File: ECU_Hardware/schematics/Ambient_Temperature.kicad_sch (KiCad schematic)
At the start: 0 parts

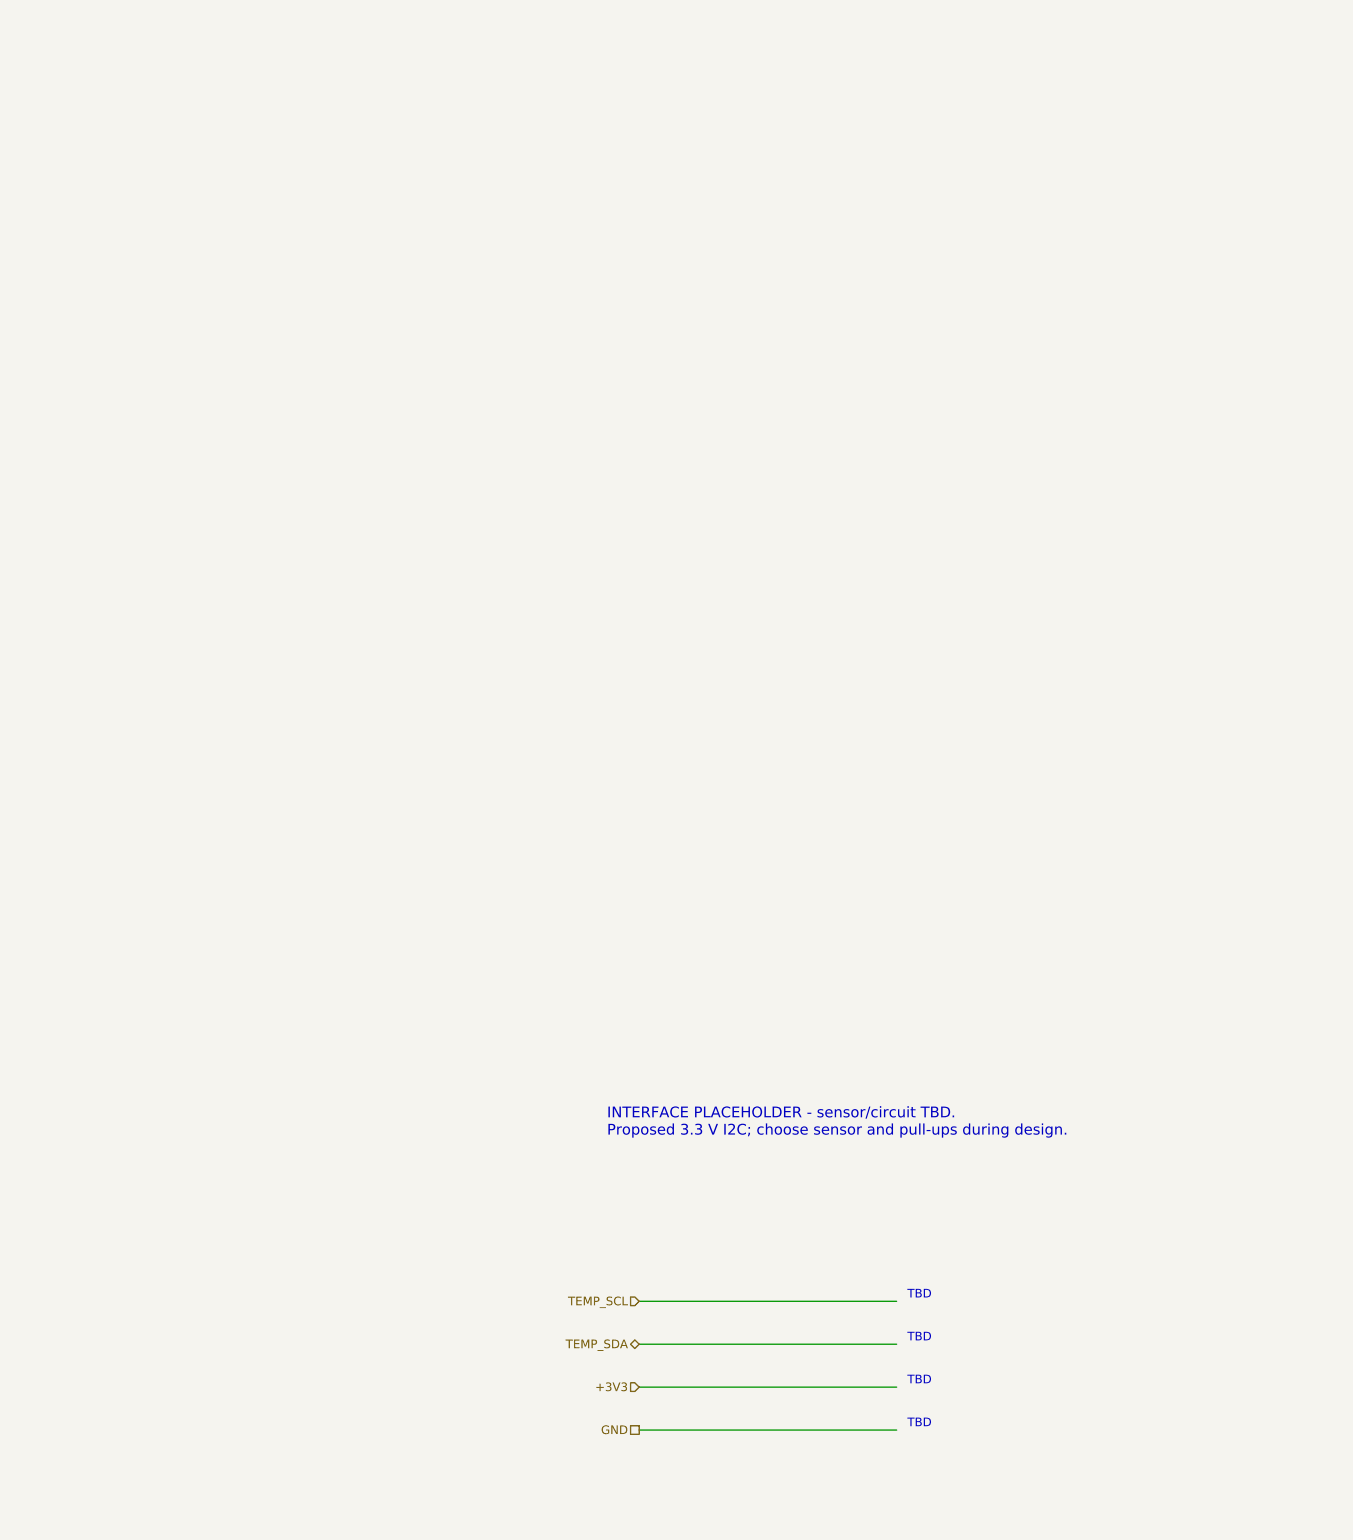
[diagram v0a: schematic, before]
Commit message: Move ECU schematics into schematics/ and add driver inputs and sensor notes
Hierarchical sheets now live in ECU_Hardware/schematics, with the new
Driver_Inputs sheet (APPS, BPPS and steering dividers and clamps), the
reviewed and JLCPCB project symbol libraries, new 3D models, and
SENSOR_INTERFACES.md with the GPS, IMU and temperature pin allocation.
The old top-level sheets and the restore backup are removed.

Claude-Session: https://claude.ai/code/session_0117trEbCv7z6CPYkN3K3GKQ
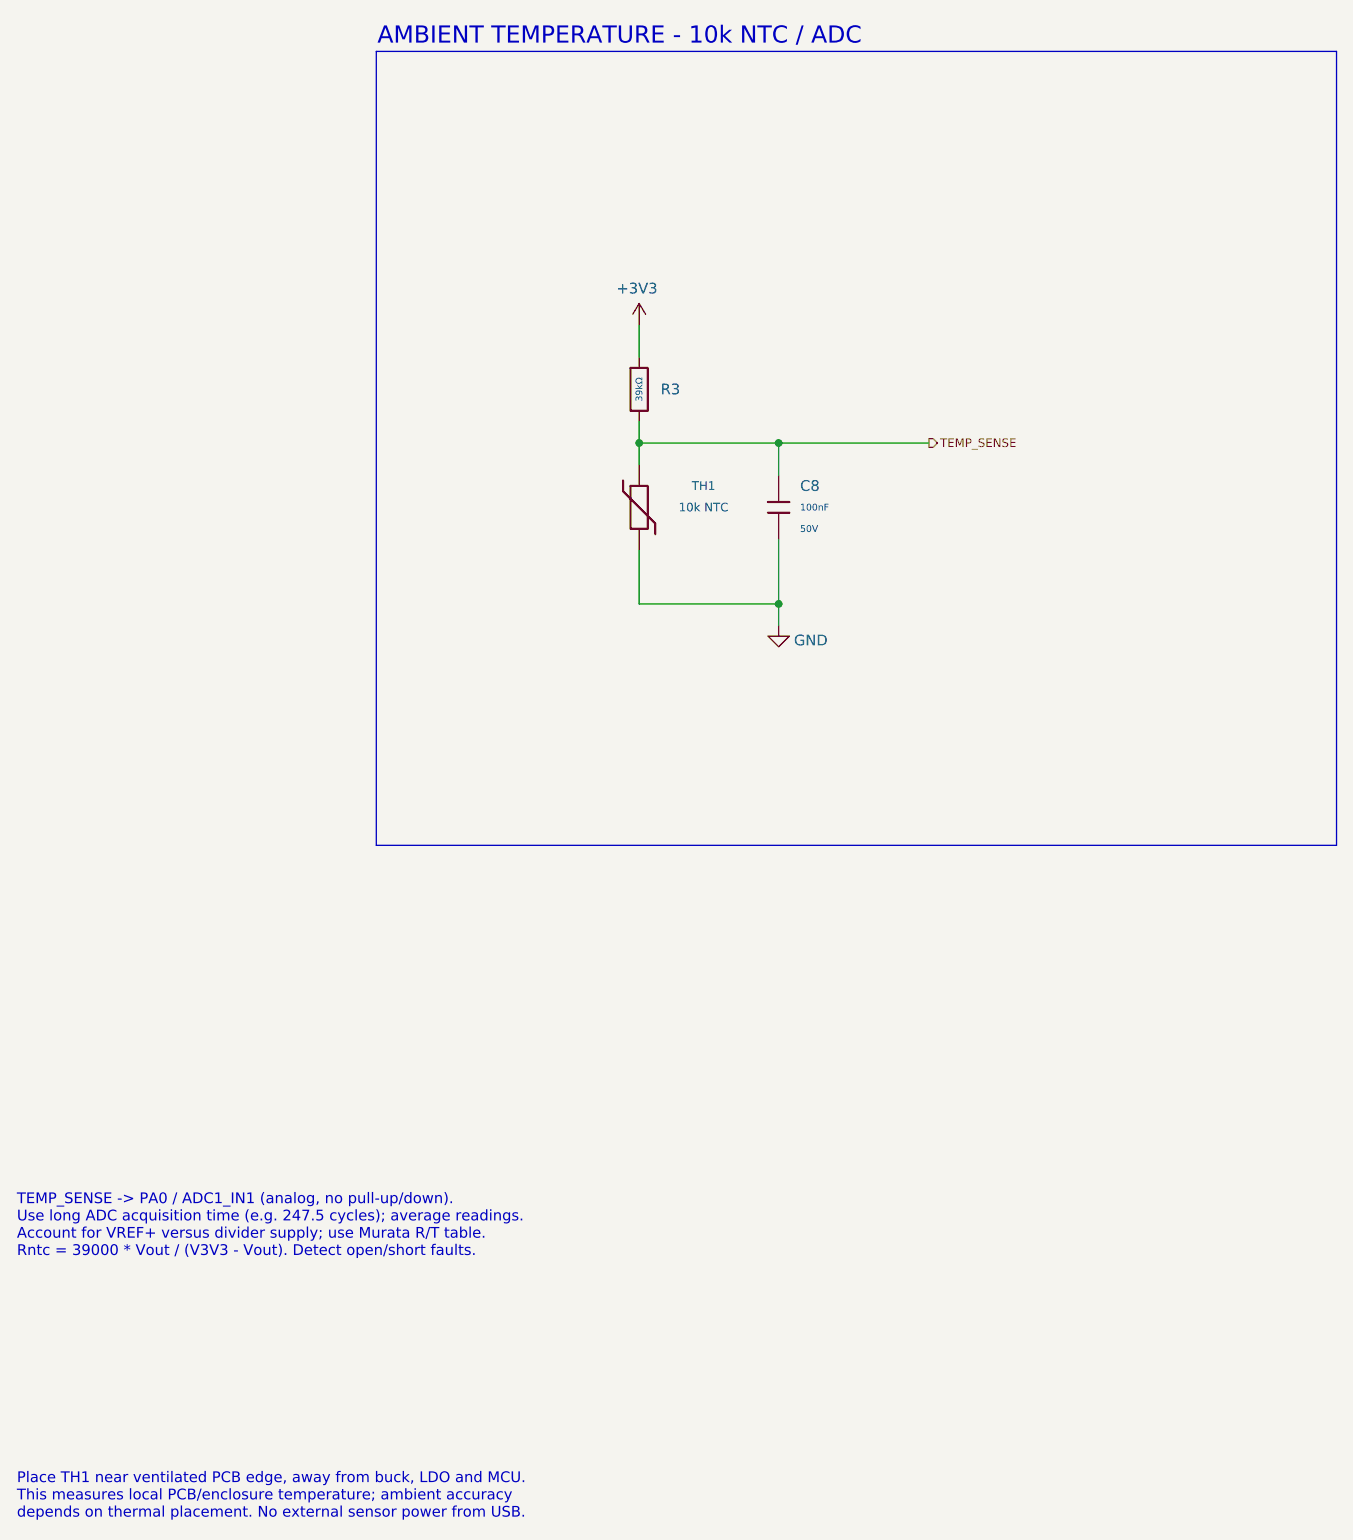
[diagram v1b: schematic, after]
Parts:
- added C8: 100nF, PCM_JLCPCB:C_0402, symbol PCM_JLCPCB-Capacitors:0402,100nF,(2)
- added R3: 39kΩ, PCM_JLCPCB:R_0402, symbol PCM_JLCPCB-Resistors:0402,39kΩ
- added TH1: 10k NTC, PCM_JLCPCB:R_0603, symbol PCM_JLCPCB-Project:NCU18XH103F60RB
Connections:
- net +3V3: now also R3.1
- net GND: now also C8.2, TH1.2
- new net TEMP_SENSE: C8.1, R3.2, TH1.1
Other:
- note added: "AMBIENT TEMPERATURE - 10k NTC / ADC"
- note added: "Place TH1 near ventilated PCB edge, away from buck, LDO and MCU. This measures local PCB/enclosure temperature; ambient accuracy depends on thermal placement. No external sensor power from USB."
- note added: "TEMP_SENSE -> PA0 / ADC1_IN1 (analog, no pull-up/down). Use long ADC acquisition time (e.g. 247.5 cycles); average readings. Account for VREF+ versus divider supply; use Murata R/T table. Rntc = 39000 * Vout / (V3V3 - Vout). Detect open/short faults."
- note removed: "INTERFACE PLACEHOLDER - sensor/circuit TBD. Proposed 3.3 V I2C; choose sensor and pull-ups during design."
- note removed: "TBD"
